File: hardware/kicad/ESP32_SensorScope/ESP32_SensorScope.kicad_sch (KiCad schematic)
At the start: 0 parts

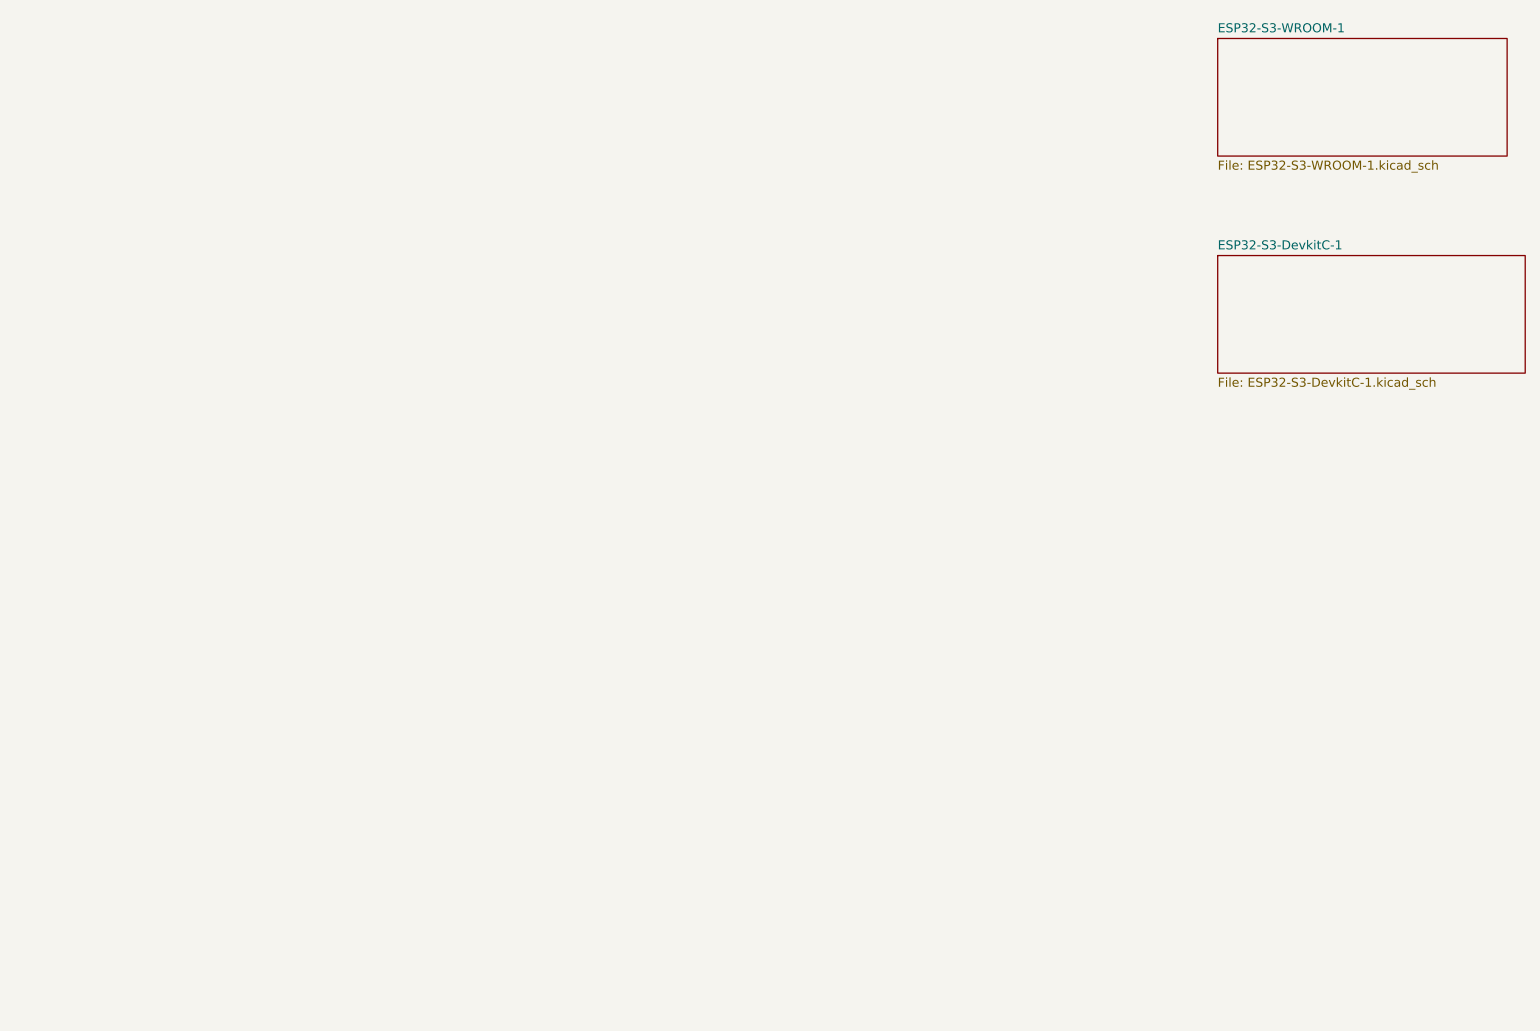
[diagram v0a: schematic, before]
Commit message: Added serial interfases
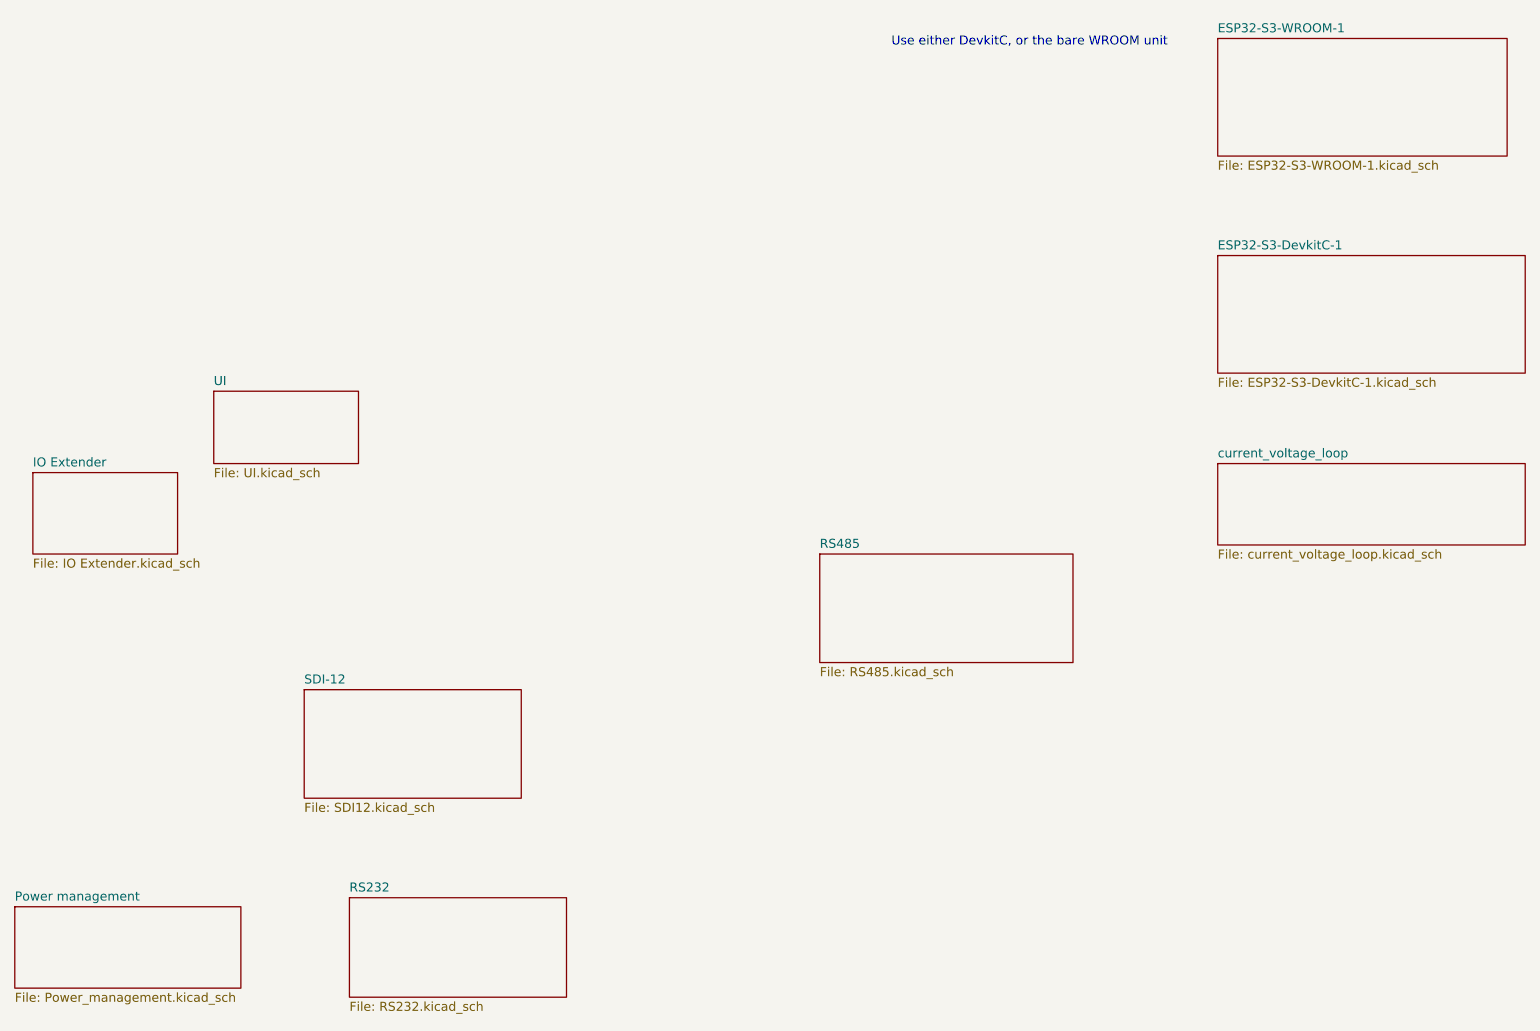
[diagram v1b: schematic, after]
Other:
- added sheet IO Extender (IO Extender.kicad_sch)
- added sheet Power management (Power_management.kicad_sch)
- added sheet RS232 (RS232.kicad_sch)
- added sheet RS485 (RS485.kicad_sch)
- added sheet SDI-12 (SDI12.kicad_sch)
- added sheet UI (UI.kicad_sch)
- added sheet current_voltage_loop (current_voltage_loop.kicad_sch)
- note added: "Use either DevkitC, or the bare WROOM unit"

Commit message: Various changes
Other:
- added sheet Scope (Scope.kicad_sch)
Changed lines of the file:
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@@
+	)
+	(sheet
+		(at 71.755 36.195)
+		(size 25.4 12.065)
+		(fields_autoplaced yes)
+		(stroke
+			(width 0.1524)
+			(type solid)
+		)
+		(fill
+			(color 0 0 0 0.0000)
+		)
+		(property "Sheetname" "Scope"
+			(at 71.755 35.4834 0)
+			(effects
+				(font
+					(size 1.27 1.27)
+				)
+				(justify left bottom)
+			)
+		)
+		(property "Sheetfile" "Scope.kicad_sch"
+			(at 71.755 48.8446 0)
+			(effects
+				(font
+					(size 1.27 1.27)
+				)
+				(justify left top)
+			)
+		)
+		(instances
+			(project "ESP32_SensorScope"
+				(path "/53b18f60-802b-4114-ad1b-2672cfed64a1"
+					(page "11")
+				)
+			)
+		)
 	)
 	(sheet

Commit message: updatet schematic
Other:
- added sheet UART (UART.kicad_sch)
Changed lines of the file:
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@@
+	)
+	(sheet
+		(at 136.398 72.898)
+		(size 15.748 8.128)
+		(fields_autoplaced yes)
+		(stroke
+			(width 0.1524)
+			(type solid)
+		)
+		(fill
+			(color 0 0 0 0.0000)
+		)
+		(property "Sheetname" "UART"
+			(at 136.398 72.1864 0)
+			(effects
+				(font
+					(size 1.27 1.27)
+				)
+				(justify left bottom)
+			)
+		)
+		(property "Sheetfile" "UART.kicad_sch"
+			(at 136.398 81.6106 0)
+			(effects
+				(font
+					(size 1.27 1.27)
+				)
+				(justify left top)
+			)
+		)
+		(instances
+			(project "ESP32_SensorScope"
+				(path "/53b18f60-802b-4114-ad1b-2672cfed64a1"
+					(page "12")
+				)
+			)
+		)
 	)
 	(sheet
